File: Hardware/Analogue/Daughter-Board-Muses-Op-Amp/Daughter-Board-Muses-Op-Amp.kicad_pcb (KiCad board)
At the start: 2 copper layers, 140.3 x 65 mm, 7 parts, among them J1 Audio In, J2 Audio Out, J4 Digital In

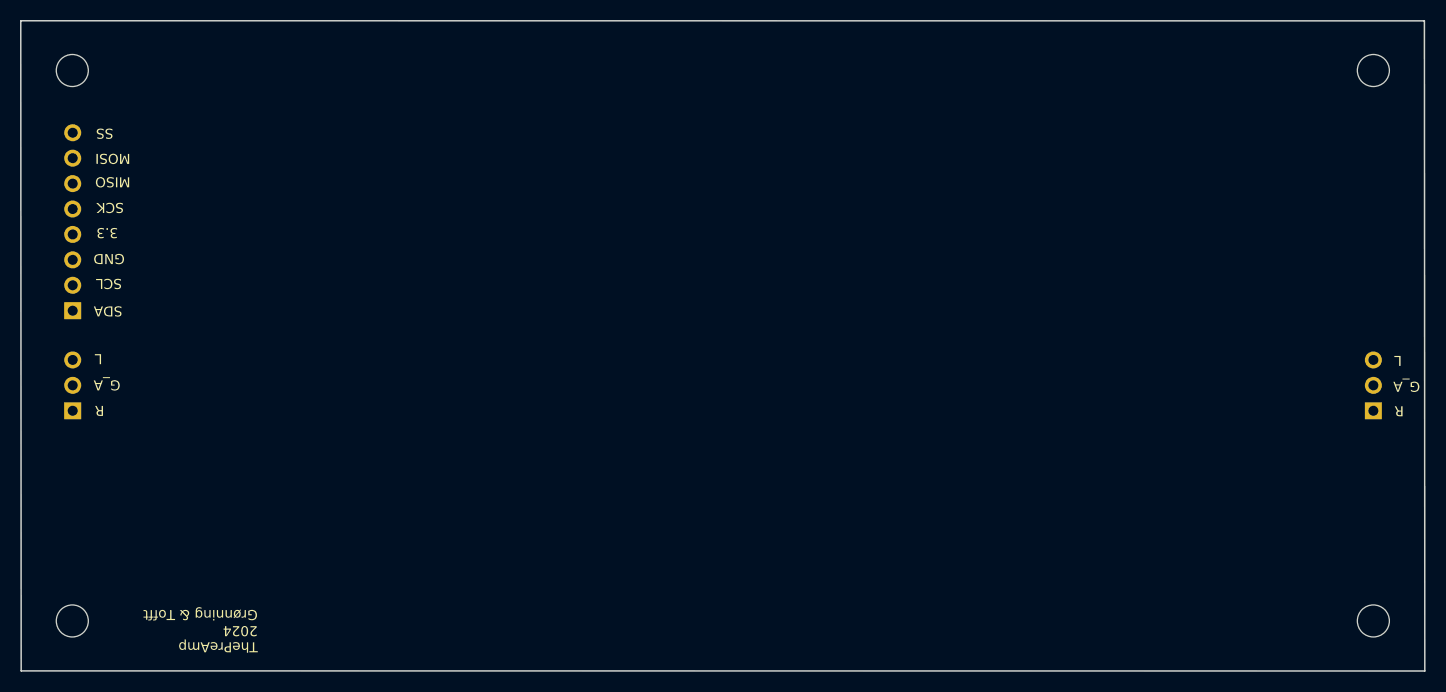
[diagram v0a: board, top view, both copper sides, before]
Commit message: PCB Daughter board started
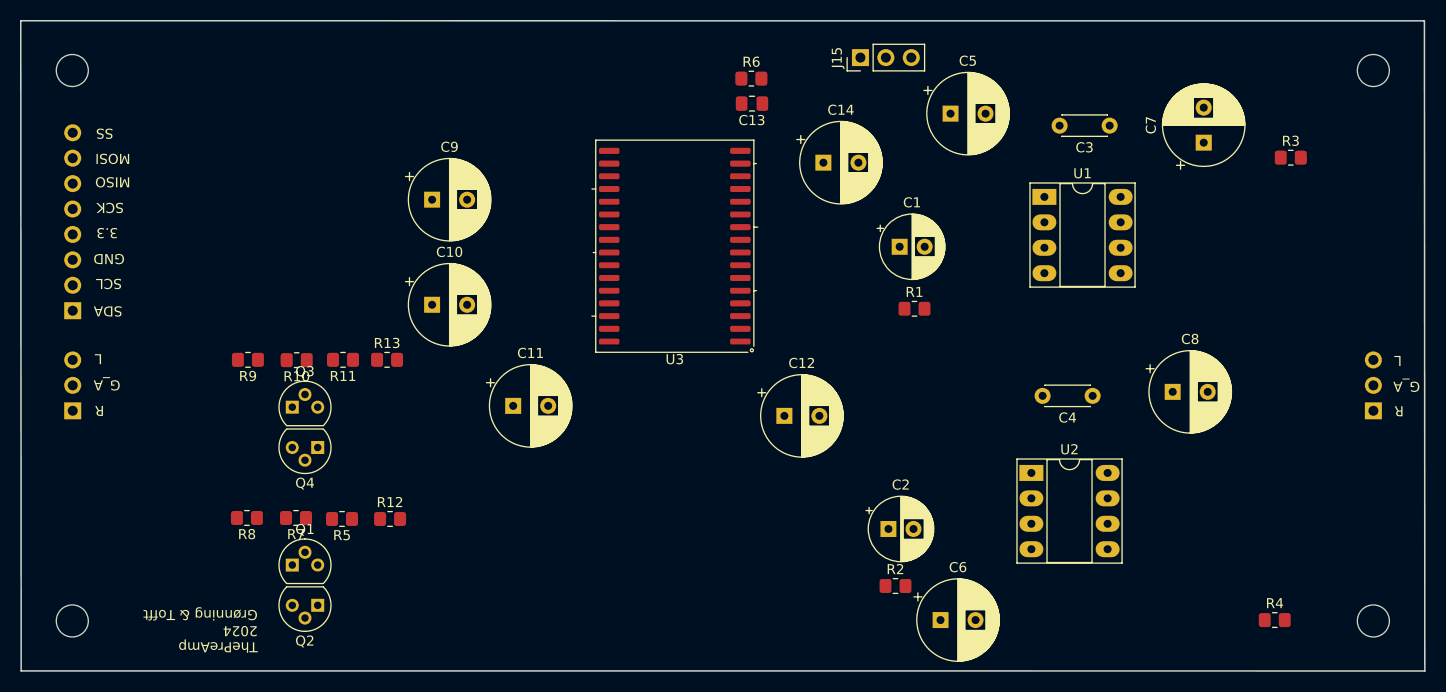
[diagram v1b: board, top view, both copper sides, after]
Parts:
- added C1: 10 uF, Capacitor_THT:CP_Radial_D6.3mm_P2.50mm, F.Cu at (174.6, 49.8)
- added C10: 100 uf/25V, Capacitor_THT:CP_Radial_D8.0mm_P3.50mm, F.Cu at (127.8, 55.6)
- added C11: 10 uf/50V, Capacitor_THT:CP_Radial_D8.0mm_P3.50mm, F.Cu at (135.9, 65.7)
- added C12: 100 uf/25V, Capacitor_THT:CP_Radial_D8.0mm_P3.50mm, F.Cu at (163.1, 66.7)
- added C13: 0,1uF, Capacitor_SMD:C_0805_2012Metric_Pad1.18x1.45mm_HandSolder, F.Cu at (159.8, 35.5)
- added C14: 100 uf/25V, Capacitor_THT:CP_Radial_D8.0mm_P3.50mm, F.Cu at (166.9, 41.4)
- added C2: 10 uF, Capacitor_THT:CP_Radial_D6.3mm_P2.50mm, F.Cu at (173.4, 78.0)
- added C3: 10 pF, Capacitor_THT:C_Disc_D4.3mm_W1.9mm_P5.00mm, F.Cu at (195.6, 37.7)
- added C4: 10 pF, Capacitor_THT:C_Disc_D4.3mm_W1.9mm_P5.00mm, F.Cu at (193.8, 64.7)
- added C5: 100 uf/25V, Capacitor_THT:CP_Radial_D8.0mm_P3.50mm, F.Cu at (179.7, 36.5)
- added C6: 100 uf/25V, Capacitor_THT:CP_Radial_D8.0mm_P3.50mm, F.Cu at (178.7, 87.1)
- added C7: 100 uf/25V, Capacitor_THT:CP_Radial_D8.0mm_P3.50mm, F.Cu at (204.9, 39.4)
- added C8: 100 uf/25V, Capacitor_THT:CP_Radial_D8.0mm_P3.50mm, F.Cu at (201.8, 64.3)
- added C9: 100 uf/25V, Capacitor_THT:CP_Radial_D8.0mm_P3.50mm, F.Cu at (127.8, 45.1)
- added J15: Buffer Power, Connector_PinHeader_2.54mm:PinHeader_1x03_P2.54mm_Vertical, F.Cu at (170.7, 30.9)
- added Q1: 2SK30, Package_TO_SOT_THT:TO-92, F.Cu at (113.9, 81.6)
- added Q2: 2SK30, Package_TO_SOT_THT:TO-92, F.Cu at (116.4, 85.7)
- added Q3: 2SK30, Package_TO_SOT_THT:TO-92, F.Cu at (113.9, 65.9)
- added Q4: 2SK30, Package_TO_SOT_THT:TO-92, F.Cu at (116.4, 69.9)
- added R1: 100K, Resistor_SMD:R_0805_2012Metric_Pad1.20x1.40mm_HandSolder, F.Cu at (176.1, 56.0)
- added R10: 220, Resistor_SMD:R_0805_2012Metric_Pad1.20x1.40mm_HandSolder, F.Cu at (114.3, 61.2)
- added R11: 220, Resistor_SMD:R_0805_2012Metric_Pad1.20x1.40mm_HandSolder, F.Cu at (119.0, 61.1)
- added R12: 1M, Resistor_SMD:R_0805_2012Metric_Pad1.20x1.40mm_HandSolder, F.Cu at (123.7, 77.0)
- added R13: 1M, Resistor_SMD:R_0805_2012Metric_Pad1.20x1.40mm_HandSolder, F.Cu at (123.3, 61.1)
- added R2: 100K, Resistor_SMD:R_0805_2012Metric_Pad1.20x1.40mm_HandSolder, F.Cu at (174.2, 83.7)
- added R3: 47, Resistor_SMD:R_0805_2012Metric_Pad1.20x1.40mm_HandSolder, F.Cu at (213.7, 40.9)
- added R4: 47, Resistor_SMD:R_0805_2012Metric_Pad1.20x1.40mm_HandSolder, F.Cu at (212.1, 87.1)
- added R5: 220, Resistor_SMD:R_0805_2012Metric_Pad1.20x1.40mm_HandSolder, F.Cu at (118.8, 77.0)
- added R6: 10, Resistor_SMD:R_0805_2012Metric_Pad1.20x1.40mm_HandSolder, F.Cu at (159.8, 33.0)
- added R7: 220, Resistor_SMD:R_0805_2012Metric_Pad1.20x1.40mm_HandSolder, F.Cu at (114.2, 76.9)
- added R8: 220K, Resistor_SMD:R_0805_2012Metric_Pad1.20x1.40mm_HandSolder, F.Cu at (109.3, 76.9)
- added R9: 220K, Resistor_SMD:R_0805_2012Metric_Pad1.20x1.40mm_HandSolder, F.Cu at (109.5, 61.1)
- added U1: NE5534, Package_DIP:DIP-8_W7.62mm_Socket_LongPads, F.Cu at (189.0, 44.9)
- added U2: NE5534, Package_DIP:DIP-8_W7.62mm_Socket_LongPads, F.Cu at (187.7, 72.4)
- added U3: Muses_72323, PCM_Package_SO_AKL:SSOP-32_11.305x20.495mm_P1.27mm, F.Cu at (152.1, 49.8)
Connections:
- J2 pad 2: GNDA_OUT -> GNDA
- J4 pad 3: GND -> GNDD

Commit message: started pcb tracks
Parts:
- moved J15 92.2 mm to (92.0, 79.0), turned to 180 degrees
- moved C12 13.1 mm to (162.1, 53.7)
- moved C9 11.0 mm to (138.0, 41.0), turned to 180 degrees
- moved C10 8.94 mm to (134.7, 49.9)
- moved C11 7.10 mm to (138.0, 58.9), turned to 180 degrees
- moved C14 6.41 mm to (162.1, 37.2)
- moved C13 5.33 mm to (157.3, 30.8)
- moved U3 4.96 mm to (149.7, 45.4)
- moved R6 2.50 mm to (157.3, 33.3)
- moved Q4 1.40 mm to (116.3, 68.5)
- moved R11 1.40 mm to (118.8, 59.7)
- moved R12 1.40 mm to (123.5, 75.6)
- moved R9 1.40 mm to (109.3, 59.7)
- moved Q3 1.40 mm to (113.8, 64.5)
- moved R13 1.40 mm to (123.2, 59.7)
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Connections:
- C4 pad 1: OUTL -> unconnected-(C4-Pad1)
- J4 pad 4: +3.3V -> +3V3
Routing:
- net +3V3: track 0.00 -> 97.1 mm
- net SPI:SS: track 0.00 -> 67.1 mm
- net SPI:SCK: track 0.00 -> 54.4 mm
- net SPI:MOSI: track 0.00 -> 52.8 mm
- net -15V: track 0.00 -> 27.4 mm
- net +15V: track 0.00 -> 16.9 mm
- net Net-(U3-D_CAP): track 0.00 -> 11.2 mm
- net Net-(U3-L_CAP): track 0.00 -> 5.90 mm
- net Net-(U3-R_CAP): track 0.00 -> 5.90 mm
- net Net-(U3-D_IN): track 0.00 -> 2.59 mm

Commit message: almost there with pcb again
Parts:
- C1, C2: footprint Capacitor_THT:CP_Radial_D6.3mm_P2.50mm -> Capacitor_THT:CP_Radial_D5.0mm_P2.00mm
- C11: footprint Capacitor_THT:CP_Radial_D8.0mm_P3.50mm -> Capacitor_THT:CP_Radial_D5.0mm_P2.00mm
- C3, C4: footprint Capacitor_THT:C_Disc_D4.3mm_W1.9mm_P5.00mm -> Capacitor_SMD:C_0805_2012Metric_Pad1.18x1.45mm_HandSolder
- Q1, Q2, Q3, Q4: value 2SK30 -> 2SK170; footprint Package_TO_SOT_THT:TO-92 -> PCM_Package_TO_SOT_THT_AKL:TO-92L_Inline
- moved R13 18.1 mm to (116.3, 43.0), turned to 90 degrees
- moved R9 17.5 mm to (113.8, 42.8), turned to 90 degrees
- moved C5 16.3 mm to (177.0, 52.6)
- moved R12 15.1 mm to (110.0, 68.9), turned to 90 degrees
- moved R11 12.6 mm to (116.3, 47.4), turned to -90 degrees
- moved R10 12.1 mm to (113.8, 47.7), turned to 90 degrees
- moved Q3 11.4 mm to (114.0, 53.1)
- moved R2 11.2 mm to (183.5, 77.5)
- moved R1 10.7 mm to (184.6, 49.5)
- moved C8 10.6 mm to (202.6, 74.9)
- moved Q4 10.3 mm to (116.4, 58.2)
- moved R4 10.2 mm to (210.8, 77.0)
- moved R3 8.95 mm to (212.0, 49.7)
- moved R5 8.91 mm to (110.0, 73.7), turned to -90 degrees
- moved C7 8.30 mm to (202.9, 47.5), turned to 0 degrees
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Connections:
- C4 pad 1: unconnected-(C4-Pad1) -> OUTL
- Q1 pad 1: Net-(Q1-S) -> +15V
- Q1 pad 3: +15V -> Net-(Q1-S)
- Q2 pad 1: -15V -> Net-(Q1-S)
- Q2 pad 3: Net-(Q1-S) -> -15V
- Q3 pad 1: Net-(Q3-S) -> +15V
- Q3 pad 3: +15V -> Net-(Q3-S)
- Q4 pad 1: -15V -> Net-(Q3-S)
- Q4 pad 3: Net-(Q3-S) -> -15V
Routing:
- net Buffer R: track 0.00 -> 68.7 mm
- net OUTL: track 0.00 -> 68.2 mm
- net OUTR: track 0.00 -> 63.0 mm
- net L-: track 0.00 -> 58.3 mm
- net L+: track 0.00 -> 45.6 mm
- net R-: track 0.00 -> 42.8 mm
- net Audio L: track 0.00 -> 33.8 mm
- net Audio L out: track 0.00 -> 30.2 mm
- net Buffer L: track 0.00 -> 30.1 mm
- net R+: track 0.00 -> 22.8 mm
- net Audio R out: track 0.00 -> 22.8 mm
- net Audio R: track 0.00 -> 20.0 mm
- net Net-(U2-+): track 0.00 -> 11.6 mm
- net Net-(U1-+): track 0.00 -> 11.1 mm
- net Net-(Q3-S): track 0.00 -> 9.96 mm
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
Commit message: pcb update
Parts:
- moved C3 8.27 mm to (184.4, 41.2)
- moved C4 7.51 mm to (184.4, 68.4)
- moved R7 6.34 mm to (113.6, 72.4)
- moved R8 6.32 mm to (113.6, 67.6)
- moved R12 6.30 mm to (116.2, 67.6)
- moved R5 6.30 mm to (116.2, 72.4)
- moved Q1 5.75 mm to (113.9, 77.9)
- moved Q2 5.73 mm to (116.3, 83.0)
- moved R1 1.50 mm to (184.5, 51.0), turned to 90 degrees
- moved R2 1.31 mm to (184.4, 78.5), turned to 90 degrees
- moved U1 1.30 mm to (187.7, 44.9)
- moved R4 1.15 mm to (212.0, 77.0)
- moved C1 1.15 mm to (176.6, 45.3)
- moved C5 1.05 mm to (175.9, 52.6)
- moved C7 0.40 mm to (202.6, 47.5)
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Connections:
- R10 pad 2: Audio L -> Audio R
- R11 pad 1: Buffer L -> Buffer R
- R12 pad 1: Buffer R -> Buffer L
- R13 pad 1: Buffer L -> Buffer R
- R5 pad 1: Buffer R -> Buffer L
- R7 pad 2: Audio R -> Audio L
- R8 pad 1: Audio R -> Audio L
- R9 pad 1: Audio L -> Audio R
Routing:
- net +15V: track 21.8 -> 236.1 mm
- net -15V: track 26.8 -> 230.3 mm
- net Buffer R: track 68.7 -> 29.9 mm
- net GNDA: track 0.00 -> 21.7 mm, vias 0 -> 11
- net Audio R: track 20.0 -> 40.0 mm
- net Buffer L: track 30.1 -> 40.1 mm
- net GNDD: track 0.00 -> 7.38 mm, vias 0 -> 4
- net R-: track 42.8 -> 36.0 mm
- net Audio L: track 33.8 -> 27.6 mm
- net L-: track 58.3 -> 52.3 mm
- net Audio L out: track 30.2 -> 25.7 mm
- net L+: track 45.6 -> 41.4 mm
- net Audio R out: track 22.8 -> 21.3 mm
- net Net-(U1-+): track 11.1 -> 12.5 mm
- net OUTL: track 68.2 -> 69.6 mm
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- added copper zone on B.Cu, net GNDA
- added copper zone on B.Cu, net GNDD
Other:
- board text removed: "This PCB is shown upside-down to have input on the left side and output on the right"

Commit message: Footprints updated - rerouting still missing
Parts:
- Q1, Q2, Q3, Q4: footprint PCM_Package_TO_SOT_THT_AKL:TO-92L_Inline -> Package_TO_SOT_THT:TO-92_HandSolder
- U3: footprint PCM_Package_SO_AKL:SSOP-32_11.305x20.495mm_P1.27mm -> Muses:TSSOP-32_6.1x11mm_P0.65mm
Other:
- board text added: "+15"
- board text added: "-15"

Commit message: PCB ready for review
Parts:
- moved C13 7.94 mm to (153.1, 37.6), turned to -90 degrees
- moved R6 4.60 mm to (155.6, 37.6), turned to 90 degrees
- moved C14 2.44 mm to (162.1, 39.6)
- moved U3 2.24 mm to (151.6, 46.7)
- moved C2 0.98 mm to (176.6, 72.8)
- moved C4 0.52 mm to (184.4, 68.9)
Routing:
- net +15V: track 236.1 -> 268.6 mm
- net +3V3: track 97.1 -> 81.8 mm
- net SPI:SCK: track 54.4 -> 62.1 mm
- net SPI:MOSI: track 52.8 -> 60.2 mm
- net Buffer L: track 40.1 -> 45.4 mm
- net Net-(U3-R_CAP): track 5.90 -> 11.2 mm
- net Buffer R: track 29.9 -> 34.4 mm
- net OUTL: track 69.6 -> 73.7 mm
- net -15V: track 230.3 -> 226.6 mm
- net Net-(U3-D_CAP): track 11.2 -> 14.6 mm
- net L+: track 41.4 -> 38.5 mm
- net SPI:SS: track 67.1 -> 64.3 mm
- net GNDD: track 7.38 -> 4.99 mm, vias 4 -> 2
- net Net-(U3-L_CAP): track 5.90 -> 8.04 mm
- net L-: track 52.3 -> 50.3 mm
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
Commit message: Small adjustments  ready to order.
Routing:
- net Net-(U1-+): track 12.5 -> 11.1 mm
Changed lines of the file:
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@@
-	)
-	(segment
-		(start 184.5 47.53)
-		(end 182.3 45.33)
-		(width 0.6)
-		(layer "F.Cu")
-		(net 1)
 	)
 	(segment
@@
 	)
 	(segment
-		(start 182.3 45.33)
-		(end 178.644888 45.33)
-		(width 0.6)
-		(layer "F.Cu")
-		(net 1)
-	)
-	(segment
 		(start 184.5 50.03)
-		(end 184.5 47.53)
+		(end 183.344888 50.03)
 		(width 0.6)
 		(layer "F.Cu")
@@
 	)
 	(segment
+		(start 183.344888 50.03)
+		(end 178.644888 45.33)
+		(width 0.6)
+		(layer "F.Cu")
+		(net 1)
+	)
+	(segment
 		(start 91.94 61.14)
 		(end 99.11 61.14)
@@
 	)
 	(segment
+		(start 155.2625 44.425)
+		(end 154.085 44.425)
+		(width 0.4)
+		(layer "F.Cu")
+		(net 5)
+	)
+	(segment
+		(start 154.085 44.425)
+		(end 153.58 44.93)
+		(width 0.4)
+		(layer "F.Cu")
+		(net 5)
+	)
+	(segment
 		(start 155.2625 45.725)
 		(end 155.2625 47.675)
@@
 	)
 	(segment
-		(start 155.2275 44.46)
-		(end 155.2625 44.425)
-		(width 0.4)
-		(layer "F.Cu")
-		(net 5)
-	)
-	(segment
 		(start 155.2625 48.975)
 		(end 156.295 48.975)
@@
 	)
 	(segment
-		(start 154.05 44.46)
-		(end 155.2275 44.46)
-		(width 0.4)
-		(layer "F.Cu")
-		(net 5)
-	)
-	(segment
 		(start 156.295 48.975)
 		(end 156.55 48.72)
@@
 		(width 0.4)
 		(layer "F.Cu")
-		(net 5)
-	)
-	(segment
-		(start 153.58 44.93)
-		(end 154.05 44.46)
-		(width 0.4)
-		(layer "F.Cu")
